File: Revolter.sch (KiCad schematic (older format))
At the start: 29 parts, among them J1 HMI, J2 TANK, J3 USB_B_Mini, J5 COND, J6 COND, J7 FAN, J8 PUMP, P3 IN+, P4 IN-, P5 MOTOR3, P6 MOTOR2, P7 MOTOR1, Q1 Q_NMOS_GSD, Q2 Q_NMOS_GSD

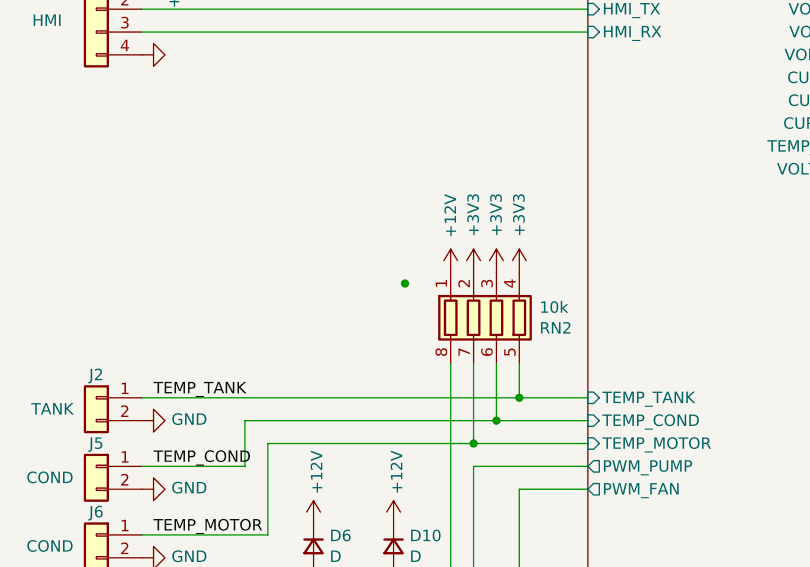
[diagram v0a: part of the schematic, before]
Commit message: - fixed EN pin of DCDC being forced to VIN (overvoltage)
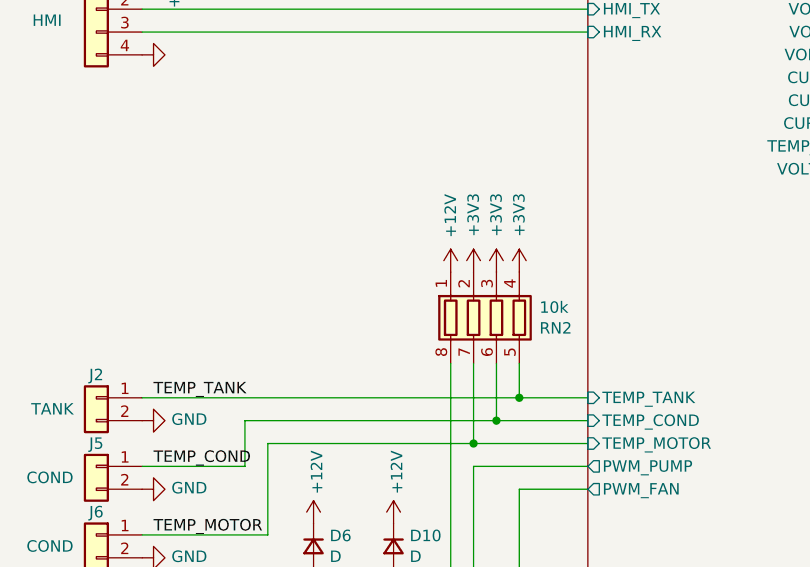
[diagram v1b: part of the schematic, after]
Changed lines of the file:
@@
 Wire Wire Line
 	2100 6100 1000 6100
-Connection ~ 2150 4300
 $EndSCHEMATC

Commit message: - switched fan MOSFET for something beefier - switched fan diode for SMC - added BOOT0 jumper - changed fan header to 3pin - removed motor thermistor - reused condenser thermistor for return temperature sensing
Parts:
- removed J6: COND, Connector_JST:JST_PH_B2B-PH-K_1x02_P2.00mm_Vertical, symbol Connector_Generic:Conn_01x02
- D6: footprint Diode_SMD:D_SOD-123 -> Diode_SMD:D_SMC
- J5: value COND -> RETURN
- J7: footprint Connector_JST:JST_PH_B2B-PH-K_1x02_P2.00mm_Vertical -> Connector_JST:JST_PH_B3B-PH-K_1x03_P2.00mm_Vertical; symbol Connector_Generic:Conn_01x02 -> Connector_Generic:Conn_01x03
- Q2: value Q_NMOS_GSD -> AON6796; footprint Package_TO_SOT_SMD:SOT-23 -> Package_SON:VSONP-8-1EP_5x6_P1.27mm; symbol Device:Q_NMOS_GSD -> Device:Q_NMOS_SGD
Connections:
- net TEMP_MOTOR is gone; now on net FAN: RN2.7 (R2.2)
- net GND: now also J7.3 (Pin_3), Q2.1 (S); no longer Q2.2 (S)
- net MCU/PWM_FAN: now also Q2.2 (G); no longer Q2.1 (G)
- net TEMP_COND renamed TEMP_RET
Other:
- moved on the sheet: J8
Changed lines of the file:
@@
 F16 "CURRENT_V" I R 4300 3500 50
 F17 "CURRENT_W" I R 4300 3600 50
-F18 "TEMP_MOTOR" I L 2950 5000 50
-F19 "TEMP_COND" I L 2950 4900 50
-F20 "VOLTAGE_DC" I R 4300 3800 50
-F21 "TEMP_MOSFET" I R 4300 3700 50
-F22 "PWM_PUMP" O L 2950 5100 50
-F23 "PWM_FAN" O L 2950 5200 50
-F24 "TEMP_TANK" I L 2950 4800 50
-F25 "HMI_TX" I L 2950 3100 50
-F26 "HMI_RX" I L 2950 3200 50
+F18 "VOLTAGE_DC" I R 4300 3800 50
+F19 "TEMP_MOSFET" I R 4300 3700 50
+F20 "PWM_PUMP" O L 2950 5100 50
+F21 "PWM_FAN" O L 2950 5200 50
+F22 "TEMP_TANK" I L 2950 4800 50
+F23 "HMI_TX" I L 2950 3100 50
+F24 "HMI_RX" I L 2950 3200 50
+F25 "TEMP_RET" I L 2950 4900 50
 $EndSheet
 $Comp
@@
 	2550 4900 2550 4650
 $Comp
-L power:+3V3 #PWR0181
-U 1 1 5EED2F4F
-P 2450 4250
-F 0 "#PWR0181" H 2450 4100 50  0001 C CNN
-F 1 "+3V3" V 2450 4500 50  0000 C CNN
-F 2 "" H 2450 4250 60  0000 C CNN
-F 3 "" H 2450 4250 60  0000 C CNN
-	1    2450 4250
-	-1   0    0    -1
-$EndComp
-$Comp
 L Device:Q_NMOS_GSD Q1
 U 1 1 5EED4311
@@
 $EndComp
 $Comp
-L Device:Q_NMOS_GSD Q2
+L Device:Q_NMOS_SGD Q2
 U 1 1 5EED647C
 P 1850 7100
 F 0 "Q2" H 2055 7146 50  0000 L CNN
-F 1 "Q_NMOS_GSD" H 2055 7055 50  0000 L CNN
-F 2 "Package_TO_SOT_SMD:SOT-23" H 2050 7200 50  0001 C CNN
+F 1 "AON6796" H 2055 7055 50  0000 L CNN
+F 2 "Package_SON:VSONP-8-1EP_5x6_P1.27mm" H 2050 7200 50  0001 C CNN
 F 3 "~" H 1850 7100 50  0001 C CNN
 	1    1850 7100
@@
 	1000 5100 1450 5100
 Wire Wire Line
-	2100 6100 2100 6550
+	2100 6250 2100 6550
 $Comp
 L power:GND #PWR0185
@@
 $EndComp
 $Comp
-L power:GND #PWR0187
-U 1 1 5EF33B60
-P 1000 5500
-F 0 "#PWR0187" H 1000 5250 50  0001 C CNN
-F 1 "GND" V 1005 5372 50  0000 R CNN
-F 2 "" H 1000 5500 50  0001 C CNN
-F 3 "" H 1000 5500 50  0001 C CNN
-	1    1000 5500
-	0    -1   -1   0
-$EndComp
-$Comp
 L power:+12V #PWR0188
 U 1 1 5EF3A20D
@@
 L power:+12V #PWR0189
 U 1 1 5EF3AED5
-P 1000 6000
-F 0 "#PWR0189" H 1000 5850 50  0001 C CNN
-F 1 "+12V" V 950 6150 50  0000 L CNN
-F 2 "" H 1000 6000 50  0001 C CNN
-F 3 "" H 1000 6000 50  0001 C CNN
-	1    1000 6000
+P 1000 6150
+F 0 "#PWR0189" H 1000 6000 50  0001 C CNN
+F 1 "+12V" V 950 6300 50  0000 L CNN
+F 2 "" H 1000 6150 50  0001 C CNN
+F 3 "" H 1000 6150 50  0001 C CNN
+	1    1000 6150
 	0    1    1    0
 $EndComp
 Text Label 1050 5100 0    50   ~ 0
-TEMP_COND
-Text Label 1050 5400 0    50   ~ 0
-TEMP_MOTOR
-Text Label 1050 6100 0    50   ~ 0
+TEMP_RET
+Text Label 1050 6250 0    50   ~ 0
 PUMP
 Text Label 1050 5800 0    50   ~ 0
@@
 Wire Wire Line
 	8150 2850 7650 2850
-Wire Wire Line
-	1550 5000 2450 5000
-Wire Wire Line
-	2450 4650 2450 5000
 $Comp
 L Device:D_Small D6
@@
 F 0 "D6" V 1704 5520 50  0000 L CNN
 F 1 "D" V 1795 5520 50  0000 L CNN
-F 2 "Diode_SMD:D_SOD-123" V 1750 5450 50  0001 C CNN
+F 2 "Diode_SMD:D_SMC" V 1750 5450 50  0001 C CNN
 F 3 "~" V 1750 5450 50  0001 C CNN
 	1    1750 5450
@@
 $EndComp
 Wire Wire Line
-	2100 5550 2100 6100
+	2100 5550 2100 6250
 $Comp
 L Connector_Generic:Conn_01x02 J2
@@
 P 800 5100
 F 0 "J5" H 800 5200 50  0000 C CNN
-F 1 "COND" H 900 5050 50  0000 L CNN
+F 1 "RETURN" H 900 5050 50  0000 L CNN
 F 2 "Connector_JST:JST_PH_B2B-PH-K_1x02_P2.00mm_Vertical" H 800 5100 50  0001 C CNN
 F 3 "~" H 800 5100 50  0001 C CNN
@@
 $EndComp
 $Comp
-L Connector_Generic:Conn_01x02 J6
-U 1 1 6055B07F
-P 800 5400
-F 0 "J6" H 800 5500 50  0000 C CNN
-F 1 "COND" H 900 5350 50  0000 L CNN
-F 2 "Connector_JST:JST_PH_B2B-PH-K_1x02_P2.00mm_Vertical" H 800 5400 50  0001 C CNN
-F 3 "~" H 800 5400 50  0001 C CNN
-	1    800  5400
-	-1   0    0    -1
-$EndComp
-$Comp
-L Connector_Generic:Conn_01x02 J7
-U 1 1 6055B67B
-P 800 5700
-F 0 "J7" H 800 5800 50  0000 C CNN
-F 1 "FAN" H 900 5650 50  0000 L CNN
-F 2 "Connector_JST:JST_PH_B2B-PH-K_1x02_P2.00mm_Vertical" H 800 5700 50  0001 C CNN
-F 3 "~" H 800 5700 50  0001 C CNN
-	1    800  5700
-	-1   0    0    -1
-$EndComp
-Wire Wire Line
-	1550 5400 1000 5400
-Wire Wire Line
-	1550 5000 1550 5400
-$Comp
 L Connector_Generic:Conn_01x02 J8
 U 1 1 6056D3E7
-P 800 6000
-F 0 "J8" H 800 6100 50  0000 C CNN
-F 1 "PUMP" H 900 5950 50  0000 L CNN
-F 2 "Connector_JST:JST_PH_B2B-PH-K_1x02_P2.00mm_Vertical" H 800 6000 50  0001 C CNN
-F 3 "~" H 800 6000 50  0001 C CNN
-	1    800  6000
+P 800 6150
+F 0 "J8" H 800 6250 50  0000 C CNN
+F 1 "PUMP" H 900 6100 50  0000 L CNN
+F 2 "Connector_JST:JST_PH_B2B-PH-K_1x02_P2.00mm_Vertical" H 800 6150 50  0001 C CNN
+F 3 "~" H 800 6150 50  0001 C CNN
+	1    800  6150
 	-1   0    0    -1
 $EndComp
@@
 Wire Wire Line
 	1750 5800 1750 6900
-Connection ~ 2450 5000
 Connection ~ 2550 4900
 Connection ~ 2650 4800
 Wire Wire Line
 	2550 4900 2950 4900
-Wire Wire Line
-	2450 5000 2950 5000
 Wire Wire Line
 	2650 4800 2950 4800
@@
 Wire Wire Line
 	2350 5800 1750 5800
-Connection ~ 2100 6100
-Wire Wire Line
-	2100 6100 1000 6100
+Connection ~ 2100 6250
+Wire Wire Line
+	2100 6250 1000 6250
+$Comp
+L Connector_Generic:Conn_01x03 J7
+U 1 1 6055B67B
+P 800 5800
+F 0 "J7" H 800 6000 50  0000 C CNN
+F 1 "FAN" H 900 5750 50  0000 L CNN
+F 2 "Connector_JST:JST_PH_B3B-PH-K_1x03_P2.00mm_Vertical" H 800 5800 50  0001 C CNN
+F 3 "~" H 800 5800 50  0001 C CNN
+	1    800  5800
+	-1   0    0    -1
+$EndComp
+$Comp
+L power:GND #PWR0173
+U 1 1 6161F173
+P 1000 5900
+F 0 "#PWR0173" H 1000 5650 50  0001 C CNN
+F 1 "GND" V 1005 5772 50  0000 R CNN
+F 2 "" H 1000 5900 50  0001 C CNN
+F 3 "" H 1000 5900 50  0001 C CNN
+	1    1000 5900
+	0    -1   -1   0
+$EndComp
+$Comp
+L power:+3V3 #PWR0181
+U 1 1 5EED2F4F
+P 2450 4250
+F 0 "#PWR0181" H 2450 4100 50  0001 C CNN
+F 1 "+3V3" V 2450 4500 50  0000 C CNN
+F 2 "" H 2450 4250 60  0000 C CNN
+F 3 "" H 2450 4250 60  0000 C CNN
+	1    2450 4250
+	-1   0    0    -1
+$EndComp
+Wire Wire Line
+	2450 4650 2350 4650
+Connection ~ 2350 4650
 $EndSCHEMATC
